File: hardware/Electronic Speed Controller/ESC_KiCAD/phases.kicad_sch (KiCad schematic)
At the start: 42 parts, among them J2 MT60, U3 LM2105DR, U4 LM2105DR, U5 LM2105DR

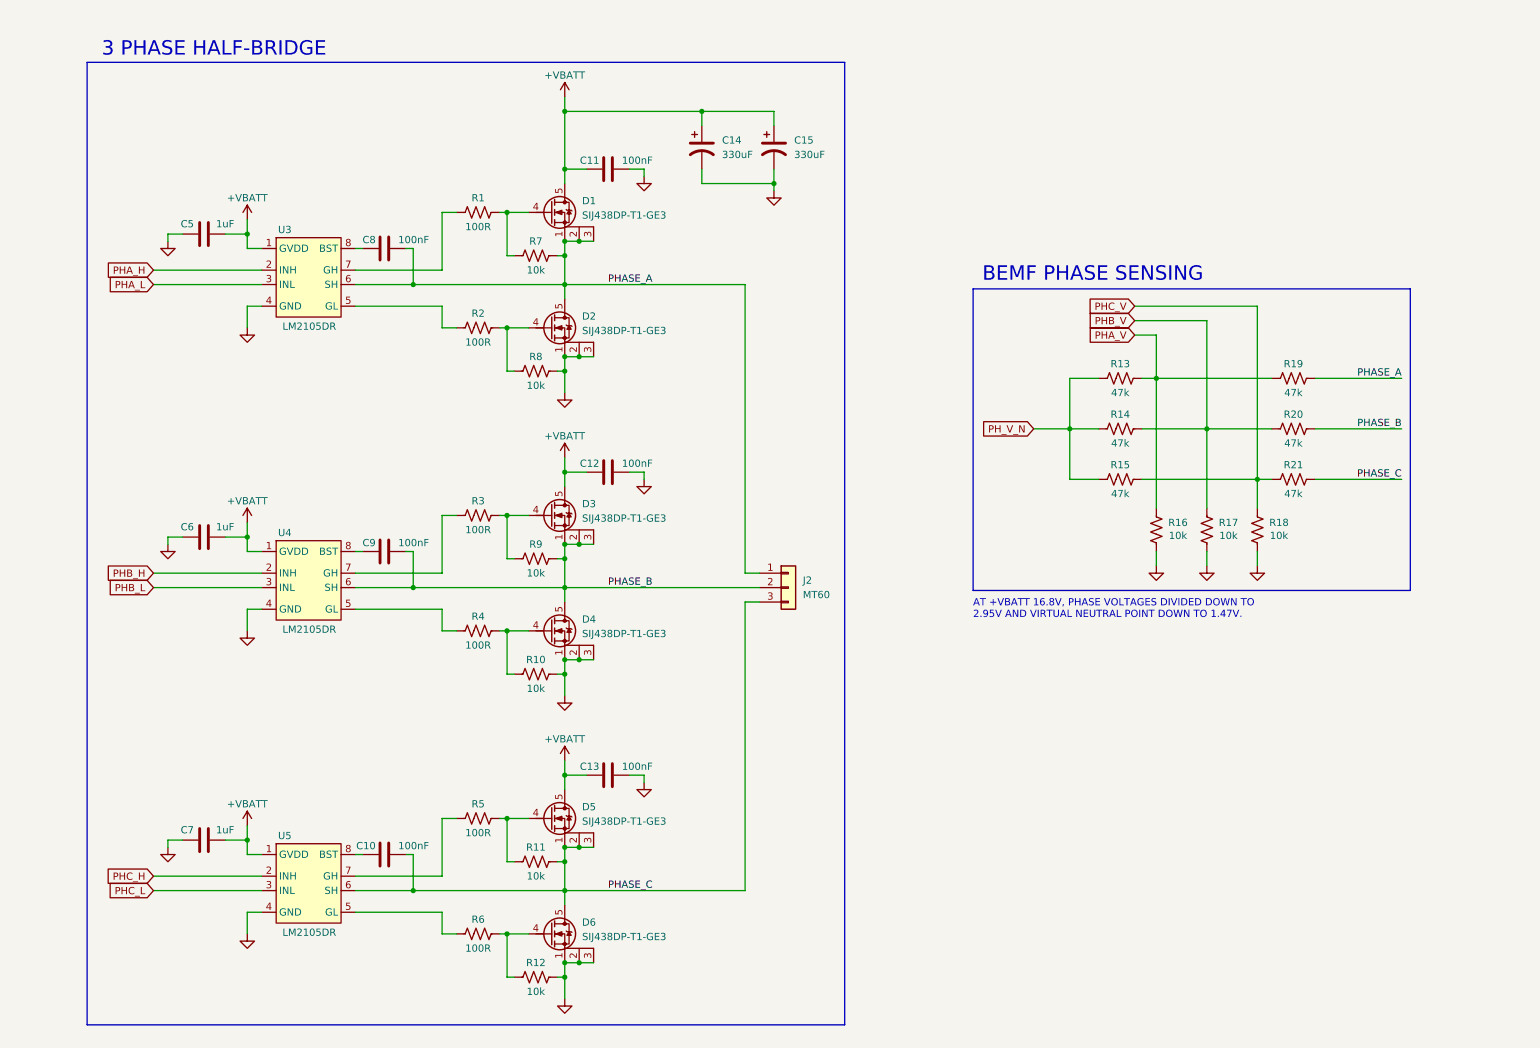
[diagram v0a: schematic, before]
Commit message: esc sensing circuitry
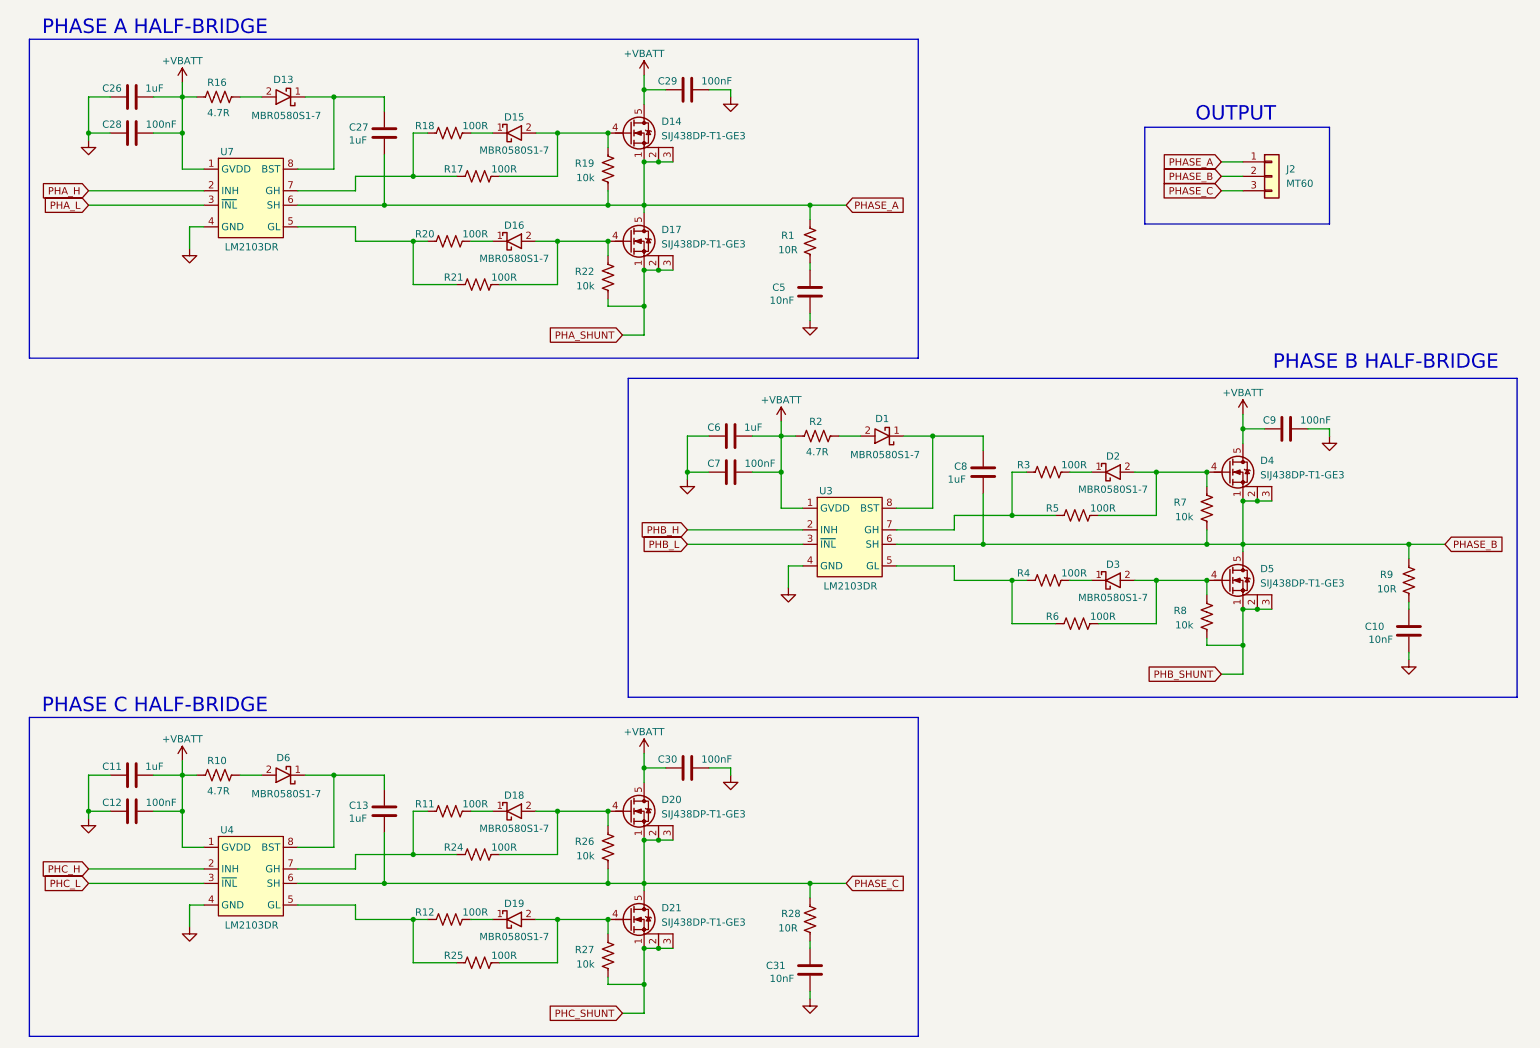
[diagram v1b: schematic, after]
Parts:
- removed C14, C15: 330uF, Capacitors:CAP_ALUM_HORIZONTAL, symbol Device:C_Polarized_US
- removed D1, D2, D3, D6: SIJ438DP-T1-GE3, Diodes:Vishay_PPAK_SO-8L, symbol Diodes:SiJ438DP
- removed R13, R14, R15: 47k, symbol Device:R_US
- removed U3, U4, U5: LM2105DR, ICs:TI_SOIC-8, symbol ICs:LM2105-D
- added C26, C27: 1uF, Capacitors:CAP_0603_1608Metric, symbol Device:C
- added C28, C29, C30: 100nF, Capacitors:CAP_0603_1608Metric, symbol Device:C
- added C31: 10nF, Capacitors:CAP_0603_1608Metric, symbol Device:C
- added D1, D13, D15, D16, D18, D19, D2, D3, D6: MBR0580S1-7, Diodes:DiodesINC_SOD123, symbol Diodes:SCHOTTKY
- added D14, D17, D20, D21: SIJ438DP-T1-GE3, Diodes:Vishay_PPAK_SO-8L, symbol Diodes:SiJ438DP
- added R22, R26, R27: 10k, Resistors:RES_0603_1608Metric, symbol Device:R_US
- added R24, R25: 100R, Resistors:RES_0603_1608Metric, symbol Device:R_US
- added R28: 10R, Resistors:RES_0603_1608Metric, symbol Device:R_US
- added U3, U4, U7: LM2103DR, ICs:TI_SOIC-8, symbol ICs:LM2103-D
- C10: value 100nF -> 10nF; footprint (none) -> Capacitors:CAP_0603_1608Metric; JLCPCB Part #  (none) -> C1589; Manufacturer (none) -> Samsung Electro-Mechanics; Manufacturer Part # (none) -> CL10B103KB8NNNC
- C11, C13, C8: value 100nF -> 1uF; footprint (none) -> Capacitors:CAP_0603_1608Metric; JLCPCB Part #  (none) -> C5673; Manufacturer (none) -> Samsung Electro-Mechanics; Manufacturer Part # (none) -> CL10A105KA8NNNC
- C12, C9: footprint (none) -> Capacitors:CAP_0603_1608Metric; JLCPCB Part # (none) -> C1591; Manufacturer (none) -> Samsung Electro-Mechanics; Manufacturer Part # (none) -> CL10B104KB8NNNC
- C5: value 1uF -> 10nF; footprint (none) -> Capacitors:CAP_0603_1608Metric; JLCPCB Part #  (none) -> C1589; Manufacturer (none) -> Samsung Electro-Mechanics; Manufacturer Part # (none) -> CL10B103KB8NNNC
- C6: footprint (none) -> Capacitors:CAP_0603_1608Metric; JLCPCB Part #  (none) -> C5673; Manufacturer (none) -> Samsung Electro-Mechanics; Manufacturer Part # (none) -> CL10A105KA8NNNC
- C7: value 1uF -> 100nF; footprint (none) -> Capacitors:CAP_0603_1608Metric; JLCPCB Part # (none) -> C1591; Manufacturer (none) -> Samsung Electro-Mechanics; Manufacturer Part # (none) -> CL10B104KB8NNNC
- D4, D5: JLCPCB Part # (none) -> C6296675; Manufacturer (none) -> Vishay Siliconix; Manufacturer Part # (none) -> SIJ438DP-T1-GE3
- J2: footprint (none) -> Connectors:CONN_MALE_TH_MT60; JLCPCB Part # (none) -> C99176; Manufacturer (none) -> Amass Electronics; Manufacturer Part # (none) -> MT60-M
- R1: value 100R -> 10R; footprint (none) -> Resistors:RES_0603_1608Metric; JLCPCB Part # (none) -> C109318; Manufacturer (none) -> YAGEO; Manufacturer Part # (none) -> RC0603FR-0710RL
- R10, R16: value 10k -> 4.7R; footprint (none) -> Resistors:RES_1206_3216Metric; JLCPCB Part # (none) -> C313986; Manufacturer (none) -> Vishay Dale; Manufacturer Part # (none) -> CRCW12064R70FKEAHP
- R11, R12, R17, R18: value 10k -> 100R; footprint (none) -> Resistors:RES_0603_1608Metric; JLCPCB Part # (none) -> C441885; Manufacturer (none) -> Panasonic Electronic Components; Manufacturer Part # (none) -> ERJ-PA3J101V
- R19: value 47k -> 10k; footprint (none) -> Resistors:RES_0603_1608Metric; JLCPCB Part # (none) -> C98220; Manufacturer (none) -> YAGEO; Manufacturer Part # (none) -> RC0603FR-0710KL
- R2: value 100R -> 4.7R; footprint (none) -> Resistors:RES_1206_3216Metric; JLCPCB Part # (none) -> C313986; Manufacturer (none) -> Vishay Dale; Manufacturer Part # (none) -> CRCW12064R70FKEAHP
- R20, R21: value 47k -> 100R; footprint (none) -> Resistors:RES_0603_1608Metric; JLCPCB Part # (none) -> C441885; Manufacturer (none) -> Panasonic Electronic Components; Manufacturer Part # (none) -> ERJ-PA3J101V
- R3, R4, R5, R6: footprint (none) -> Resistors:RES_0603_1608Metric; JLCPCB Part # (none) -> C441885; Manufacturer (none) -> Panasonic Electronic Components; Manufacturer Part # (none) -> ERJ-PA3J101V
- R7, R8: footprint (none) -> Resistors:RES_0603_1608Metric; JLCPCB Part # (none) -> C98220; Manufacturer (none) -> YAGEO; Manufacturer Part # (none) -> RC0603FR-0710KL
- R9: value 10k -> 10R; footprint (none) -> Resistors:RES_0603_1608Metric; JLCPCB Part # (none) -> C109318; Manufacturer (none) -> YAGEO; Manufacturer Part # (none) -> RC0603FR-0710RL
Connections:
- net +VBATT: now also C11.2, C12.2, C9.1, D4.5 (D), R10.1, R16.1, R2.1, C26.2, C28.2, C29.1, C30.1, D14.5 (D), D20.5 (D), U3.1 (GVDD), U4.1 (GVDD), U7.1 (GVDD); no longer C11.1, C12.1, C13.1, C5.2, D5.5 (D)
- net GND: now also C10.1, C11.1, C12.1, C9.2, C26.1, C28.1, C29.2, C30.2, C31.1, U3.4 (GND), U4.4 (GND), U7.4 (GND); no longer C11.2, C12.2, C13.2, D4.1 (S), D4.2 (S), D4.3 (S), R10.2, R12.2, R16.1, R17.1, R18.1, R8.2
- net PHASE_A: now also R1.1, C27.1, D14.1 (S), D14.2 (S), D14.3 (S), D17.5 (D), U7.6 (SH); no longer C8.2, R7.2
- net PHASE_B: now also C8.1, D4.1 (S), D4.2 (S), D4.3 (S), D5.5 (D), R7.2, R9.1, U3.6 (SH); no longer C9.2, D4.5 (D), R20.2, R9.2
- net PHASE_C: now also C13.1, D20.1 (S), D20.2 (S), D20.3 (S), D21.5 (D), R26.2, R28.1, U4.6 (SH); no longer C10.2, D5.1 (S), D5.2 (S), D5.3 (S), R11.2, R21.2
- net PHA_H: now also U7.2 (INH)
- net PHA_L: now also U7.3 (~{INL})
- net PHB_H: now also U3.2 (INH)
- net PHB_L: now also U3.3 (~{INL})
- net PHC_H: now also U4.2 (INH)
- net PHC_L: now also U4.3 (~{INL})
- net at R3.1: now also R5.1, U3.7 (GH)
- net at R3.2: now also D2.1 (K); no longer R9.1
- net at R7.1: now also D4.4 (G), R5.2, D2.2 (A); no longer R1.2
- net at R12.1: now also R25.1, U4.5 (GL); no longer R6.2
- net at R8.1: now also D5.4 (G), R6.2, D3.2 (A); no longer R2.2
- net at R6.1: now also R4.1, U3.5 (GL)
- net PHA_V: no longer names the net of R19.1
- net PHA_V: now also R17.2, D14.4 (G), D15.2 (A); no longer R16.2
- net PHB_V: no longer names the net of R20.1
- net PHB_V: now also R21.1, U7.5 (GL); no longer R17.2
- net PHC_V: no longer names the net of R18.2
- net PHC_V: now also D15.1 (K); no longer R21.1
- new net: C31.2, R28.2
- new net: R11.1, R24.1, U4.7 (GH)
- new net: C13.2, D6.1 (K), U4.8 (BST)
- new net: C10.2, R9.2
- new net: D3.1 (K), R4.2
- new net: C5.2, R1.2
- new net: R17.1, R18.1, U7.7 (GH)
- new net: D19.2 (A), D21.4 (G), R25.2, R27.1
- new net: C27.2, D13.1 (K), U7.8 (BST)
- new net: D16.2 (A), D17.4 (G), R21.2, R22.1
- new net: D18.2 (A), D20.4 (G), R24.2, R26.1
- new net: D18.1 (K), R11.2
- new net: D19.1 (K), R12.2
- new net: D6.2 (A), R10.2
- new net: D16.1 (K), R20.2
- new net: D13.2 (A), R16.2
- new net: C8.2, D1.1 (K), U3.8 (BST)
- new net: D1.2 (A), R2.2
- new net PHA_SHUNT: D17.1 (S), D17.2 (S), D17.3 (S), R22.2
- new net PHB_SHUNT: D5.1 (S), D5.2 (S), D5.3 (S), R8.2
- new net PHC_SHUNT: D21.1 (S), D21.2 (S), D21.3 (S), R27.2
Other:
- note added: "OUTPUT"
- note added: "PHASE A HALF-BRIDGE"
- note added: "PHASE B HALF-BRIDGE"
- note added: "PHASE C HALF-BRIDGE"
- note removed: "3 PHASE HALF-BRIDGE"
- note removed: "AT +VBATT 16.8V, PHASE VOLTAGES DIVIDED DOWN TO 2.95V AND VIRTUAL NEUTRAL POINT DOWN TO 1.47V."
- note removed: "BEMF PHASE SENSING"
- title: (none) -> 3 PHASE H-BRIDGE
- moved on the sheet: J2

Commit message: update FCC stm32 ioc file
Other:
- title: 3 PHASE H-BRIDGE -> 3 PHASE HALF-BRIDGE
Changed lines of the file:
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@@
 	(paper "A4")
 	(title_block
-		(title "3 PHASE H-BRIDGE")
+		(title "3 PHASE HALF-BRIDGE")
 		(comment 1 "REVIEWED BY:")
 		(comment 3 "GITHUB: /nikphillydev")
